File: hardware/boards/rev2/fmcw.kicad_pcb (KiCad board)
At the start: 4 copper layers, 94.6 x 83.4 mm, 446 parts, among them CON1 BARREL_JACK, J1 SD_Card, J2 USB_B_Micro, J3 SMA, J4 SMA, J5 SMA, J6 Conn_02x08_Odd_Even, Q1 DNP(RE1C002UN), Q2 RE1C002UN, SW1 SW_PUSH, T1 uwave, T2 uwave, T3 uwave, T4 uwave, T5 uwave, T6 uwave, T7 uwave, T8 uwave, U1 LP5907MFX-3.3, U10 LP5907MFX-3.0, U11 LTC2292, U12 ADF4158, U13 TLV172DCK, U14 PAT1220-C-3DB, U15 HMC431, U16 PD4859J5050S2HF, U17 PAT1220-C-5DB, U18 SE5004L, U2 LP5907MFX-1.8, U20 PAT1220-C-6DB, U21 LMV321, U22 TRF37A73, U23 SKY65404, U24 TRF37A73, U25 SKY65404, U26 L7980, U27 L7980, U28 L7980, U29 LP2985A-10DBVR, U3 KT2520K-T, U30 TPS7A91, U31 TPS7A91, U32 TPS7A91, U33 LP5907MFX-3.0, U34 TPS7A91, U35 5400BL15B050E, U36 5400BL15B050E, U37 5400BL15B050E, U38 ADL5802, U39 ADA4940-2, U4 NC7SVU04P5X, U40 TPS7A91, U5 NB3N551, U6 XC7A15T-FTG256, U7 W25Q32JV, U8 93LCxxBxxOT, U9 FT2232H, Y1 12MHz

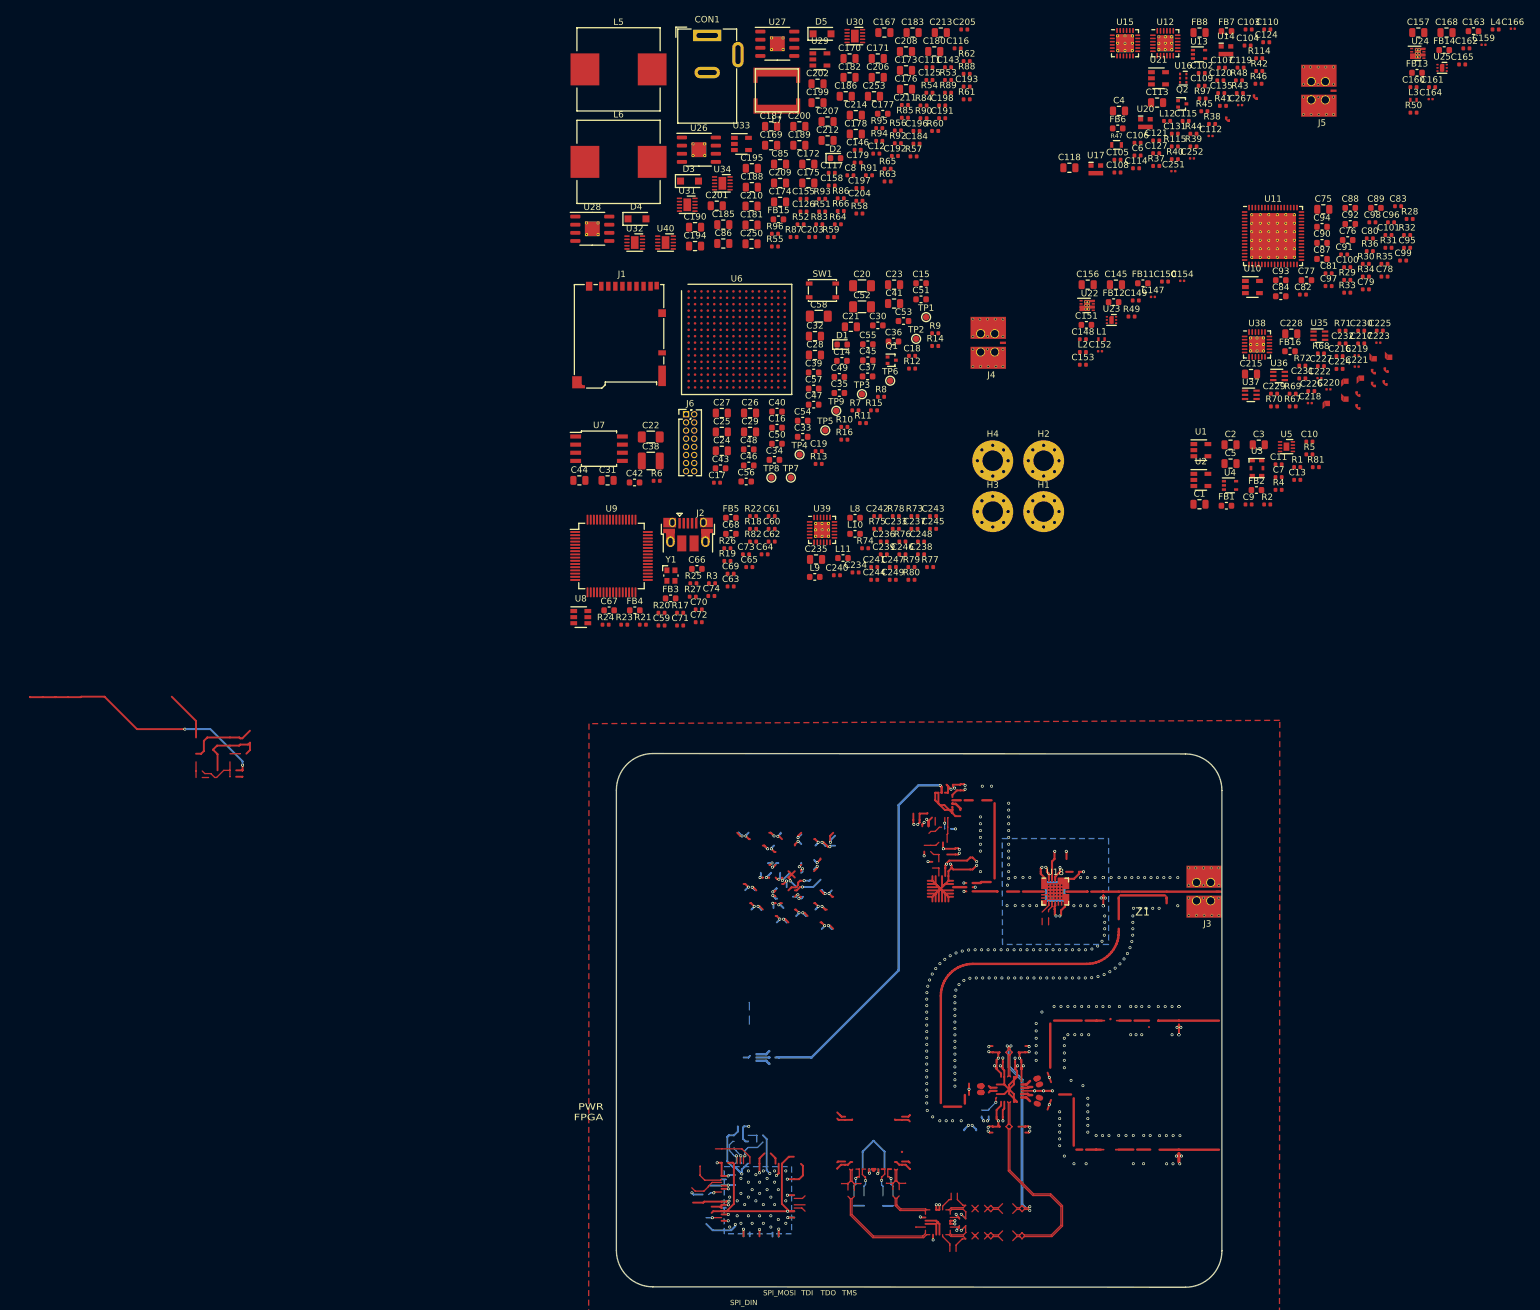
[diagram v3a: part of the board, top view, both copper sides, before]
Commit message: replace v5 footprints
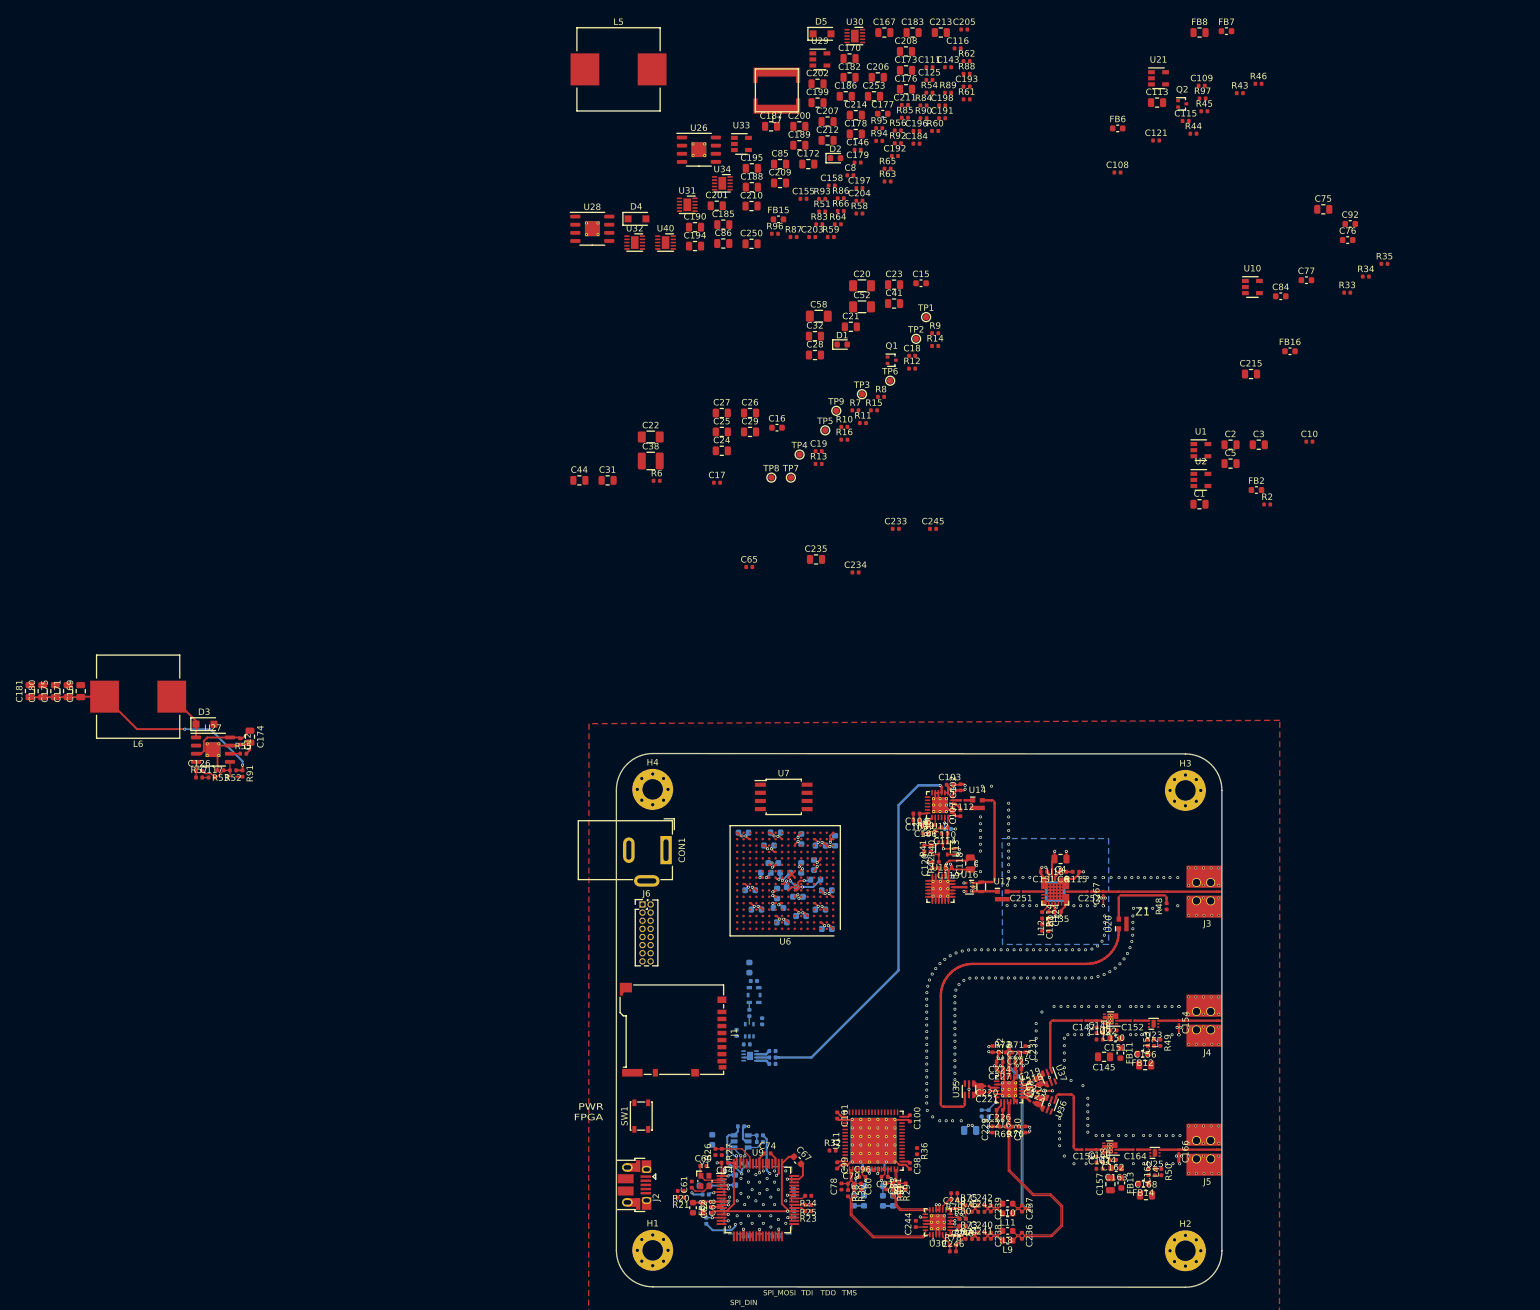
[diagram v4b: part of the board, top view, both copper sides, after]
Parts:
- C11, C13, C14, C228, C247, C30, C33, C34, C35, C36, C37, C39, C40, C42, C43, C45, C46, C47, C48, C49, C50, C51, C53, C54, C55, C56, C57, C59, C63, C66, C69, C7, C70, C71, C72, C73, C87, C88, C89, C9, C90, C91, C93, C94, C95, FB1, FB4, FB5, R1, R17, R18, R19, R22, R3, R37, R4, R5, R67, R68, R81, R82, U3, U4, U5, U8: moved to B.Cu
- moved C168 187.6 mm to (185.0, 112.5)
- moved L4 186.5 mm to (185.4, 108.9), turned to 270 degrees
- moved C157 186.2 mm to (179.4, 110.8), turned to 90 degrees
- moved C163 186.2 mm to (180.3, 108.3), turned to 180 degrees
- moved C159 183.5 mm to (175.3, 105.4), turned to 180 degrees
- moved FB14 183.2 mm to (184.6, 110.7), turned to 180 degrees
- moved C166 183.0 mm to (190.1, 105.7), turned to 270 degrees
- moved C162 182.2 mm to (179.8, 107.0), turned to 180 degrees
- moved C165 179.5 mm to (186.4, 108.9), turned to 90 degrees
- moved FB13 179.5 mm to (181.1, 110.6), turned to 270 degrees
- moved U24 177.6 mm to (179.3, 105.1), turned to 180 degrees
- moved C161 176.8 mm to (177.7, 108.4)
- moved R28 175.7 mm to (138.4, 112.2), turned to 270 degrees
- moved U25 175.3 mm to (186.4, 105.9), turned to 180 degrees
- moved C160 175.0 mm to (177.7, 107.4)
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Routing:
- net /if/IF1+: track 0.00 -> 36.0 mm, vias 0 -> 2
- net /IF1+: track 36.0 -> 0.00 mm, vias 2 -> 0
- net /if/IF1-: track 0.00 -> 35.6 mm, vias 0 -> 2
- net /IF1-: track 35.6 -> 0.00 mm, vias 2 -> 0
- net /if/IF2+: track 0.00 -> 33.8 mm
- net /IF2+: track 33.8 -> 0.00 mm
- net /if/IF2-: track 0.00 -> 33.4 mm
- net /IF2-: track 33.4 -> 0.00 mm
- net /fpga/usb/3V3_IO: track 46.6 -> 30.2 mm, vias 8 -> 7
- net /power/12V: track 0.00 -> 11.0 mm
- net GND: track 243.5 -> 237.7 mm, vias 353 -> 351
- net Net-(R22-Pad1): track 2.40 -> 7.91 mm, vias 1 -> 2
- net Net-(C247-Pad2): track 0.00 -> 3.38 mm
- net Net-(C247-Pad1): track 3.38 -> 0.00 mm
- net Net-(C90-Pad1): track 5.01 -> 6.58 mm
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
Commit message: finish placement and routing
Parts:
- removed C15: 470n, Capacitor_SMD:C_0603_1608Metric
- removed JP17, JP2, JP4: balun_exit_inv, fmcw_v5:balun_exit_inv
- removed JP18, JP3, JP5: balun_exit, fmcw_v5:balun_exit
- added T10: uwave, fmcw_v5:balun_exit_inv, F.Cu at (158.2, 96.4)
- added T11: uwave, fmcw_v5:balun_exit_inv, F.Cu at (169.0, 94.0)
- added T12: uwave, fmcw_v5:balun_exit_inv, F.Cu at (169.3, 97.7)
- added T13: uwave, fmcw_v5:balun_exit, F.Cu at (169.3, 94.8)
- added T14: uwave, fmcw_v5:balun_exit, F.Cu at (169.0, 98.5)
- added T9: uwave, fmcw_v5:balun_exit, F.Cu at (158.2, 95.6)
- C1, C108, C109, C111, C113, C116, C117, C12, C121, C125, C126, C143, C146, C155, C158, C172, C174, C176, C177, C179, C183, C184, C187, C190, C191, C192, C193, C194, C195, C196, C197, C198, C199, C2, C200, C201, C202, C203, C204, C205, C206, C207, C208, C209, C210, C211, C212, C213, C214, C22, C248, C250, C253, C26, C28, C29, C3, C31, C32, C38, C41, C44, C5, C52, C75, C77, C8, C84, C85, C86, D3, D4, D5, FB6, FB8, Q2, R10, R12, R13, R15, R16, R32, R33, R34, R36, R43, R44, R45, R46, R52, R53, R54, R55, R56, R57, R58, R59, R60, R61, R62, R63, R64, R65, R66, R7, R8, R83, R84, R85, R86, R87, R88, R89, R90, R91, R92, R93, R94, R95, R96, R97, U1, U10, U2, U21, U26, U27, U28, U29, U33: moved to B.Cu
- C11, C13, C7, C9, FB1, R1, R4, R5, R81, U3, U4, U5: moved to F.Cu
- J6: footprint Connector_PinHeader_1.27mm:PinHeader_2x08_P1.27mm_Vertical -> Connector_PinHeader_2.54mm:PinHeader_2x07_P2.54mm_Vertical
- L7: footprint fmcw_v5:SRR6040A -> fmcw_v5:L_Bourns_SRR6040A
- TP1, TP2, TP3, TP4, TP5, TP6, TP7, TP8, TP9: footprint TestPoint:TestPoint_Pad_D1.0mm -> TestPoint:TestPoint_Loop_D1.80mm_Drill1.0mm_Beaded
- U30, U31, U32, U34, U40: footprint Package_DFN_QFN:Texas_S-PDSO-N10_EP1.2x2mm -> Package_DFN_QFN:Texas_S-PDSO-N10_EP1.2x2mm_ThermalVias; moved to B.Cu
- moved C92 171.6 mm to (131.0, 109.3), turned to 90 degrees
- moved R34 163.0 mm to (132.2, 106.8), turned to 180 degrees
- moved C76 160.3 mm to (147.1, 107.8), turned to 270 degrees
- moved R35 159.9 mm to (145.5, 107.3), turned to 270 degrees
- moved R33 157.6 mm to (132.2, 104.8), turned to 180 degrees
- moved TP1 147.0 mm to (92.7, 110.5)
- moved C213 145.4 mm to (107.7, 69.1)
- moved FB8 145.3 mm to (160.1, 72.3), turned to 180 degrees
- moved C10 143.7 mm to (124.2, 109.7), turned to 270 degrees
- moved TP2 141.9 mm to (96.4, 110.5)
- moved C75 140.8 mm to (116.7, 61.4)
- moved R46 140.0 mm to (153.4, 70.0), turned to 90 degrees
- moved R62 139.9 mm to (110.5, 67.3), turned to 90 degrees
- moved R43 139.7 mm to (148.8, 70.5), turned to 270 degrees
- moved C205 139.4 mm to (124.2, 66.0), turned to 180 degrees
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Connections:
- C218 pad 2: Net-(C218-Pad2) -> /mixer/RF1a-
- C219 pad 2: Net-(C219-Pad2) -> /mixer/RF1a+
- C222 pad 2: Net-(C222-Pad2) -> /mixer/RF2a-
- C223 pad 2: Net-(C223-Pad2) -> /mixer/RF2a+
- J6 pad 10: /3V3D -> /fpga/EXT2_4
- J6 pad 11: /fpga/EXT2_1 -> /fpga/EXT2_2
- J6 pad 12: /fpga/EXT2_4 -> /fpga/EXT2_5
- J6 pad 13: /fpga/EXT2_2 -> /fpga/EXT2_3
- J6 pad 14: /fpga/EXT2_5 -> /fpga/EXT2_6
- J6 pad 9: GND -> /fpga/EXT2_1
- R4 pad 1: /FPGA_REF -> /ADF_REF
- R5 pad 1: /ADC_REF -> /FPGA_REF
- R81 pad 1: /ADF_REF -> /ADC_REF
- U22 pad 3: (no net) -> GND
- U22 pad 4: (no net) -> GND
- U22 pad 6: (no net) -> GND
- U22 pad 8: (no net) -> GND
- U24 pad 3: (no net) -> GND
- U24 pad 4: (no net) -> GND
- U24 pad 6: (no net) -> GND
- U24 pad 8: (no net) -> GND
- U35 pad 3: Net-(JP17-Pad1) -> /mixer/LOIa-
- U35 pad 4: Net-(JP18-Pad1) -> /mixer/LOIa+
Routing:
- net GND: track 237.7 -> 555.8 mm, vias 351 -> 484
- net /3V3D: track 29.4 -> 286.8 mm, vias 17 -> 49
- net /3V0: track 0.00 -> 154.9 mm, vias 0 -> 8
- net /1V0: track 4.58 -> 125.5 mm, vias 3 -> 17
- net /3V3A: track 17.2 -> 133.0 mm, vias 10 -> 12
- net /power/12V: track 11.0 -> 124.9 mm, vias 0 -> 6
- net /fpga/adc/3V0: track 5.53 -> 105.8 mm, vias 2 -> 5
- net /3V6: track 0.00 -> 90.6 mm, vias 0 -> 16
- net Net-(C3-Pad1): track 0.00 -> 87.0 mm, vias 0 -> 1
- net /fpga/SPI_MOSI: track 0.00 -> 83.3 mm, vias 0 -> 1
- net Net-(C5-Pad1): track 0.00 -> 72.5 mm, vias 0 -> 1
- net /fpga/TCK: track 0.00 -> 71.9 mm, vias 0 -> 8
- net /fpga/CCLK: track 0.00 -> 71.2 mm, vias 0 -> 2
- net /fpga/PROGRAM_B: track 0.00 -> 68.2 mm, vias 0 -> 6
- net /fpga/SPI_DIN: track 0.00 -> 67.0 mm, vias 0 -> 1
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- added copper zone on In2.Cu, net /3V3A
- added copper zone on In2.Cu, net /3V3D
- removed copper zone on In2.Cu, net /fpga/usb/3V3_IO
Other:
- board size 94.6 x 83.4 mm -> 118.6 x 83.2 mm
- board text added: "PCB cost (OshPark 4-layer): $10/sq.in. x 3.28in. x 4.67in. = $153"
- board text removed: "PCB cost (OshPark 4-layer): $10/sq.in. x 3.28in. x 3.72in. = $122"
